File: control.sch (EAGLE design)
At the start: 103 parts, among them CN1 40PIN FPC, CN2 MINI B USB, CN3 0530471210, SW1 TACT, SW10 TACT, SW11 TACT, SW12 TACT, SW13 TACT, SW14 TACT, SW15 TACT, SW16 TACT, SW2 TACT, SW3 TACT, SW4 TACT, SW5 TACT, SW6 TACT, SW7 TACT, SW8 TACT, SW9 TACT, U1 STM32H743ZI, U2 AS4C8M16SA, U3 TPS61169DCKR, U4 USBLC6-2SC6, U5 FT230X, U6 DCDC 3V3

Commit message: Control nearly done
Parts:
- removed TP1, TP2: TEST_POINT_SQUARE, MISC:TEST_POINT_SQUARE
- added CN4: 2X10 HEADER, CONNECTORs:2X10_HEADER
- added R21: 10R, r_0603:ERJ3EKF10R0V
- CN3: value 0530471210 -> 2X10 HEADER; device CONNECTORs:PICOBLADE_12_TH_V -> CONNECTORs:2X10_HEADER
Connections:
- net JTAG_TRACECLK renamed N$5
- net JTAG_TRACED0 renamed N$6
- removed net 3V3D: CN3.3, CN3.4
- removed net DGND: CN3.10, CN3.11, CN3.12
- removed net DISP_!DE: CN1.34, U1.PF10
- removed net DISP_STBY: CN1.31
- removed net JTAG_TRACE: U1.PB3
- removed net N$101: U1.PB2
- removed net N$103: U1.PB4
- removed net N$111: U1.PB12
- removed net N$112: U1.PB13
- removed net N$120: U1.PC5
- removed net N$123: U1.PC8
- removed net N$128: U1.PC13
- removed net N$129: U1.PC14
- removed net N$130: U1.PC15
- removed net N$142: U1.PD11
- removed net N$143: U1.PD12
- removed net N$144: U1.PD13
- removed net N$169: U1.PF9
- removed net N$170: U1.PF8
- removed net N$171: U1.PF7
- removed net N$191: U1.PG3
- removed net N$192: U1.PG2
- removed net N$3: U1.PC4
- removed net N$47: C27.2, R3.1
- removed net N$49: C28.2, R4.1
- removed net N$5 (its old number): TP2.P$1, U6.VIN-
- removed net N$51: C29.2, R5.1
- removed net N$53: C30.2, R6.1
- removed net N$55: C31.2, R7.1
- removed net N$57: C32.2, R8.1
- removed net N$59: C33.2, R9.1
- removed net N$61: C34.2, R10.1
- removed net N$63: C35.2, R11.1
- removed net N$65: C36.2, R12.1
- removed net N$67: C37.2, R13.1
- removed net N$69: C38.2, R14.1
- removed net N$71: C39.2, R15.1
- removed net N$73: C40.2, R16.1
- removed net N$75: C41.2, R17.1
- removed net N$77: C42.2, R18.1
- new net BTN_0: C40.2, R16.1, U1.PC15
- new net BTN_1: C31.2, R7.1, U1.PD11
- new net BTN_2: C34.2, R10.1, R21.2, U1.PF9
- new net BTN_3: C37.2, R13.1, U1.PF7
- new net BTN_4: C30.2, R6.1, U1.PD12
- new net BTN_5: C33.2, R9.1, U1.PB12
- new net BTN_6: C36.2, R12.1, U1.PC4
- new net BTN_7: C29.2, R5.1, U1.PD13
- new net BTN_8: C32.2, R8.1, U1.PB13
- new net BTN_9: C35.2, R11.1, U1.PF8
- new net BTN_AMPS: C41.2, R17.1, U1.PC13
- new net BTN_CANCEL: C38.2, R14.1, U1.PC14
- new net BTN_DP: C39.2, R15.1, U1.PC5
- new net BTN_ON0FF: C27.2, R3.1, U1.PG3
- new net BTN_OUT_CONT: C28.2, R4.1, U1.PG2
- new net BTN_VOLTS: C42.2, R18.1, U1.PB2
- new net DISP_EN: CN1.31, U1.PC8
- new net JTAG_TDO: CN3.7, U1.PB3
- new net JTAG_TRST: CN3.2, U1.PB4
- new net PGND: CN4.10, CN4.11, CN4.12, CN4.9, U6.VIN-
- new net VIN: CN4.13, CN4.14, CN4.7, CN4.8, U6.VIN+
- net 3V3: now also CN3.1, CN4.19, CN4.2
- net ADC_!DRDY: now also CN4.5; no longer CN3.7
- net ADC_SPI_!CS: now also CN4.15; no longer CN3.8
- net ADC_SPI_MISO: now also CN4.4; no longer CN3.6
- net ADC_SPI_MOSI: now also CN4.3; no longer CN3.5
- net ADC_SPI_SCLK: now also CN4.6; no longer CN3.9
- net DAC_I2C_SCL: now also CN4.17; no longer CN3.1
- net DAC_I2C_SDA: now also CN4.18; no longer CN3.2
- net DISP_DE: now also CN1.34, U1.PF10; no longer U1.PF6
- net GND: now also CN3.11, CN3.12, CN3.13, CN3.14, CN3.15, CN3.16, CN3.17, CN3.18, CN3.19, CN3.6, CN4.1, CN4.16, CN4.20
- net JTAG_TCK: now also CN3.5
- net JTAG_TDI: now also CN3.3
- net JTAG_TMS: now also CN3.4
- net N$4: now also U1.PF6; no longer TP1.P$1, U6.VIN+
- net STM_BOOT0: now also R21.1
- net STM_NRST: now also CN3.8

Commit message: Checked against Cube
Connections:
- removed net N$104: U1.PB5
- removed net N$125: U1.PC10
- removed net N$126: U1.PC11
- removed net N$127: U1.PC12
- removed net N$133: U1.PD2
- removed net N$135: U1.PD4
- removed net N$136: U1.PD5
- removed net N$138: U1.PD7
- removed net N$161: U1.PE1
- removed net N$162: U1.PE0
- removed net N$180: U1.PG14
- removed net N$183: U1.PG11
- removed net N$4: U1.PF6
- removed net N$5: U1.PE2
- removed net N$6: U1.PE3
- removed net N$84: U1.PC1
- removed net N$95: U1.PA12
- net ADC_!DRDY: now also U1.PC1
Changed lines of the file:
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@@
-</segment>
-</net>
-<net name="N$95" class="0">
-<segment>
-<pinref part="U1" gate="G$1" pin="PA12"/>
-<wire x1="104.14" y1="226.06" x2="73.66" y2="226.06" width="0.1524" layer="91"/>
 </segment>
 </net>
@@
 </segment>
 </net>
-<net name="N$104" class="0">
-<segment>
-<pinref part="U1" gate="G$1" pin="PB5"/>
-<wire x1="104.14" y1="200.66" x2="73.66" y2="200.66" width="0.1524" layer="91"/>
-</segment>
-</net>
 <net name="DAC_I2C_SCL" class="0">
 <segment>
@@
 </segment>
 </net>
-<net name="N$125" class="0">
-<segment>
-<pinref part="U1" gate="G$1" pin="PC10"/>
-<wire x1="104.14" y1="144.78" x2="73.66" y2="144.78" width="0.1524" layer="91"/>
-</segment>
-</net>
-<net name="N$126" class="0">
-<segment>
-<pinref part="U1" gate="G$1" pin="PC11"/>
-<wire x1="104.14" y1="142.24" x2="73.66" y2="142.24" width="0.1524" layer="91"/>
-</segment>
-</net>
-<net name="N$127" class="0">
-<segment>
-<pinref part="U1" gate="G$1" pin="PC12"/>
-<wire x1="104.14" y1="139.7" x2="73.66" y2="139.7" width="0.1524" layer="91"/>
-</segment>
-</net>
 <net name="BTN_AMPS" class="0">
 <segment>
@@
 </segment>
 </net>
-<net name="N$133" class="0">
-<segment>
-<pinref part="U1" gate="G$1" pin="PD2"/>
-<wire x1="104.14" y1="121.92" x2="73.66" y2="121.92" width="0.1524" layer="91"/>
-</segment>
-</net>
-<net name="N$135" class="0">
-<segment>
-<pinref part="U1" gate="G$1" pin="PD4"/>
-<wire x1="104.14" y1="116.84" x2="73.66" y2="116.84" width="0.1524" layer="91"/>
-</segment>
-</net>
-<net name="N$136" class="0">
-<segment>
-<pinref part="U1" gate="G$1" pin="PD5"/>
-<wire x1="104.14" y1="114.3" x2="73.66" y2="114.3" width="0.1524" layer="91"/>
-</segment>
-</net>
-<net name="N$138" class="0">
-<segment>
-<pinref part="U1" gate="G$1" pin="PD7"/>
-<wire x1="104.14" y1="109.22" x2="73.66" y2="109.22" width="0.1524" layer="91"/>
-</segment>
-</net>
 <net name="SDRAM_D13" class="0">
 <segment>
@@
 </segment>
 </net>
-<net name="N$161" class="0">
-<segment>
-<pinref part="U1" gate="G$1" pin="PE1"/>
-<wire x1="144.78" y1="124.46" x2="175.26" y2="124.46" width="0.1524" layer="91"/>
-</segment>
-</net>
-<net name="N$162" class="0">
-<segment>
-<pinref part="U1" gate="G$1" pin="PE0"/>
-<wire x1="144.78" y1="127" x2="175.26" y2="127" width="0.1524" layer="91"/>
-</segment>
-</net>
 <net name="SDRAM_A9" class="0">
 <segment>
@@
 </segment>
 </net>
-<net name="N$180" class="0">
-<segment>
-<pinref part="U1" gate="G$1" pin="PG14"/>
-<wire x1="144.78" y1="177.8" x2="175.26" y2="177.8" width="0.1524" layer="91"/>
-</segment>
-</net>
-<net name="N$183" class="0">
-<segment>
-<pinref part="U1" gate="G$1" pin="PG11"/>
-<wire x1="144.78" y1="185.42" x2="175.26" y2="185.42" width="0.1524" layer="91"/>
-</segment>
-</net>
 <net name="ADC_SPI_!CS" class="0">
 <segment>
@@
 <wire x1="289.56" y1="177.8" x2="259.08" y2="177.8" width="0.1524" layer="91"/>
 <label x="261.62" y="177.8" size="1.778" layer="95"/>
-</segment>
-</net>
-<net name="N$84" class="0">
-<segment>
-<pinref part="U1" gate="G$1" pin="PC1"/>
-<wire x1="104.14" y1="167.64" x2="73.66" y2="167.64" width="0.1524" layer="91"/>
 </segment>
 </net>
@@
 <label x="205.74" y="431.8" size="1.778" layer="95"/>
 </segment>
+<segment>
+<pinref part="U1" gate="G$1" pin="PC1"/>
+<wire x1="104.14" y1="167.64" x2="73.66" y2="167.64" width="0.1524" layer="91"/>
+<label x="76.2" y="167.64" size="1.778" layer="95"/>
+</segment>
 </net>
 <net name="BTN_6" class="0">
@@
 </segment>
 </net>
-<net name="N$4" class="0">
-<segment>
-<pinref part="U1" gate="G$1" pin="PF6"/>
-<wire x1="144.78" y1="154.94" x2="175.26" y2="154.94" width="0.1524" layer="91"/>
-</segment>
-</net>
-<net name="N$5" class="0">
-<segment>
-<pinref part="U1" gate="G$1" pin="PE2"/>
-<wire x1="144.78" y1="121.92" x2="175.26" y2="121.92" width="0.1524" layer="91"/>
-</segment>
-</net>
-<net name="N$6" class="0">
-<segment>
-<pinref part="U1" gate="G$1" pin="PE3"/>
-<wire x1="144.78" y1="119.38" x2="175.26" y2="119.38" width="0.1524" layer="91"/>
-</segment>
-</net>

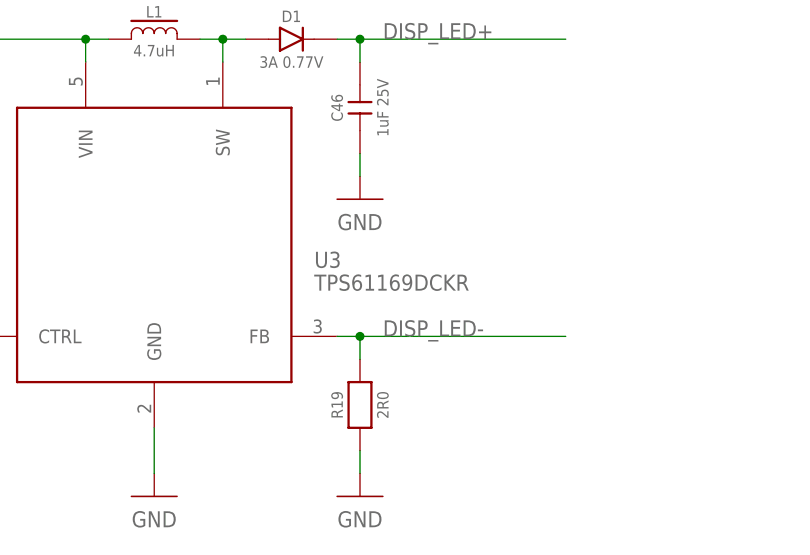
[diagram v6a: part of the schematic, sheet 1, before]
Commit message: Updated libs with digikey numbers
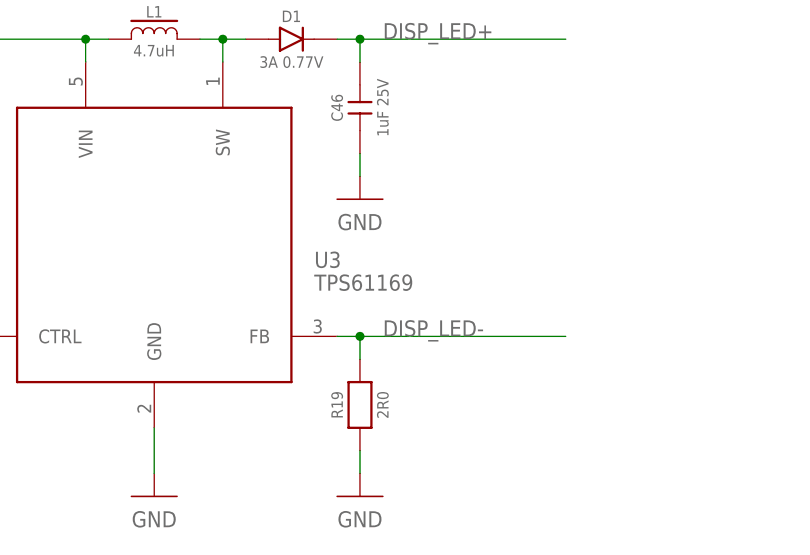
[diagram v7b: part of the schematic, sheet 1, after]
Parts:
- C45: device CAPACITORS:GRM188R60J475ME19D -> CAPACITORS:CL10B475KQ8NQNC
- U3: value TPS61169DCKR -> TPS61169
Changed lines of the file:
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@@
 <part name="GND49" library="NETS" deviceset="GND" device=""/>
 <part name="U$42" library="NETS" deviceset="3V3" device=""/>
-<part name="U3" library="ICs" deviceset="TPS61169" device="DCKR"/>
+<part name="U3" library="ICs" deviceset="TPS61169" device="DCKR" value="TPS61169"/>
 <part name="U6" library="ICs" deviceset="PDQE15-Q24-S3-D" device="" value="DCDC 3V3"/>
-<part name="C45" library="CAPACITORS" deviceset="GRM188R60J475ME19D" device="" value="4.7uF 6.3V"/>
+<part name="C45" library="CAPACITORS" deviceset="CL10B475KQ8NQNC" device="" value="4.7uF 6.3V"/>
 <part name="GND50" library="NETS" deviceset="GND" device=""/>
 <part name="GND51" library="NETS" deviceset="GND" device=""/>

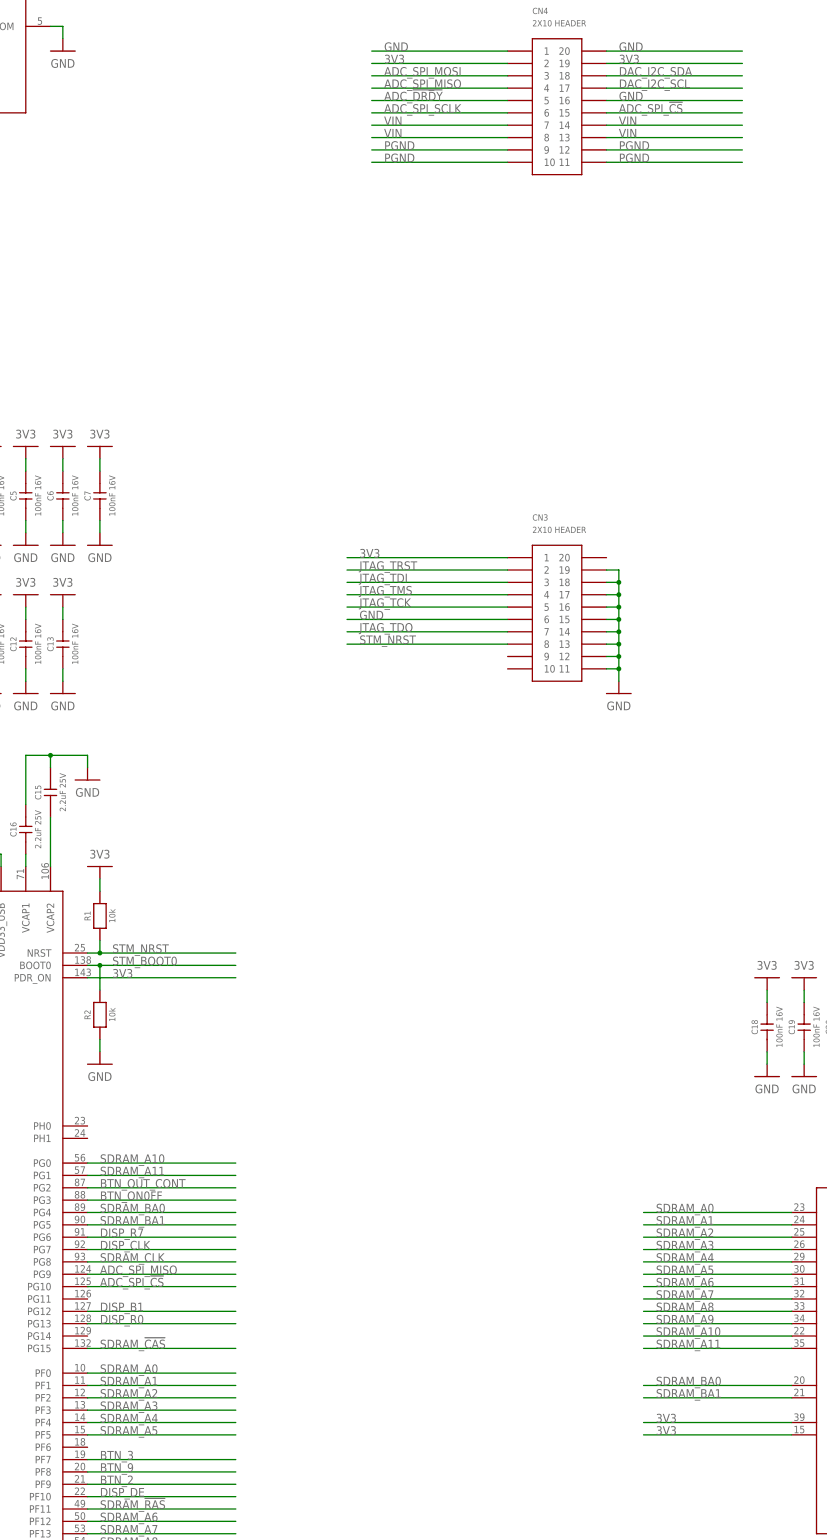
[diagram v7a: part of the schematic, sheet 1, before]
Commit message: Added control for the output relay
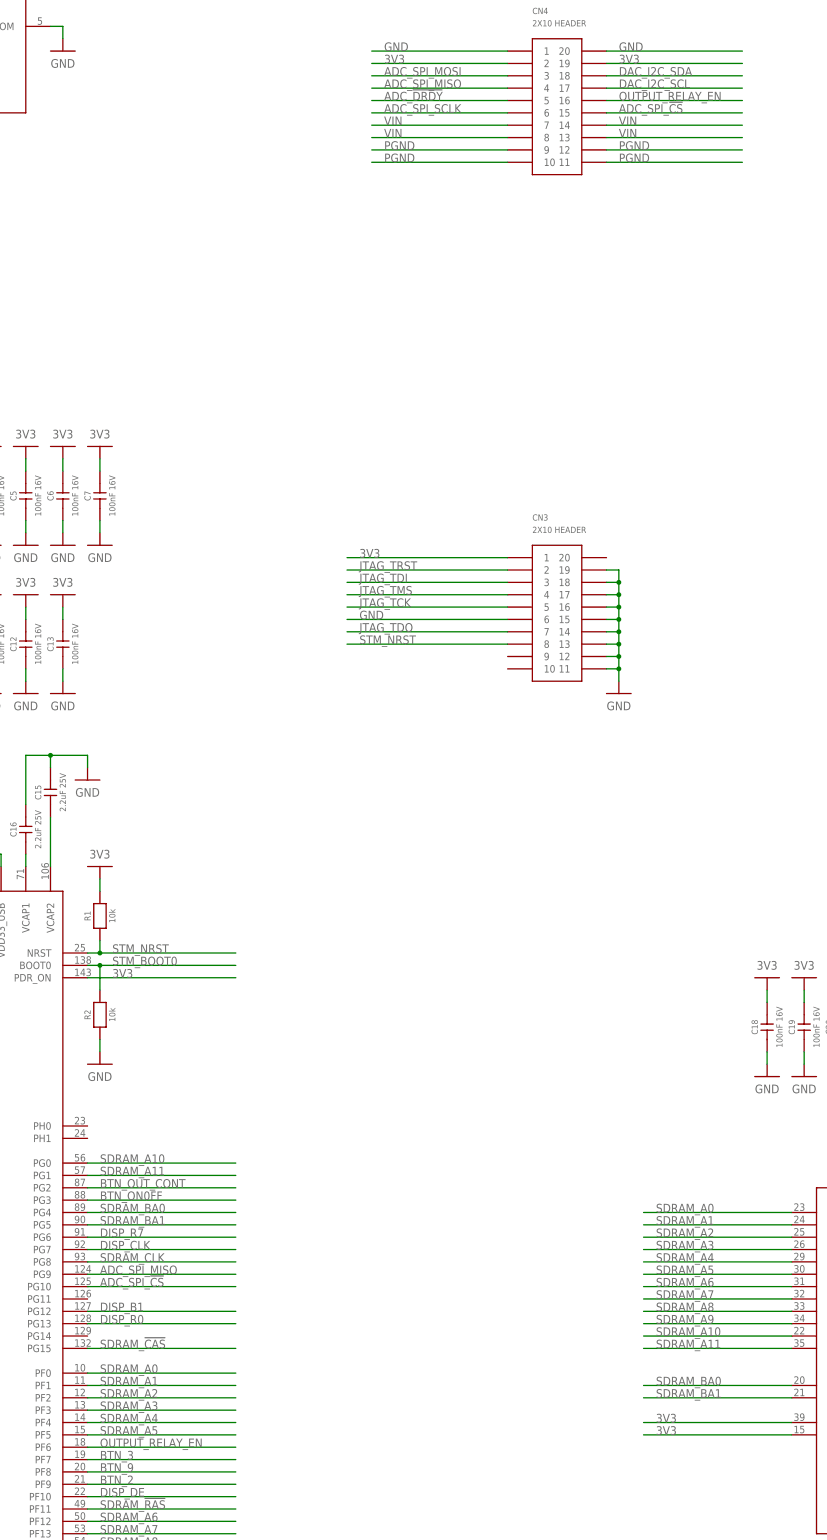
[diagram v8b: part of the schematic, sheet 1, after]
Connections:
- new net OUTPUT_RELAY_EN: CN4.16, U1.PF6
- net GND: no longer CN4.16
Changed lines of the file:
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@@
-</segment>
-<segment>
-<pinref part="CN4" gate="G$1" pin="16"/>
-<wire x1="251.46" y1="431.8" x2="279.4" y2="431.8" width="0.1524" layer="91"/>
-<label x="254" y="431.8" size="1.778" layer="95"/>
 </segment>
 <segment>
@@
 </segment>
 </net>
+<net name="OUTPUT_RELAY_EN" class="0">
+<segment>
+<pinref part="CN4" gate="G$1" pin="16"/>
+<wire x1="251.46" y1="431.8" x2="279.4" y2="431.8" width="0.1524" layer="91"/>
+<label x="254" y="431.8" size="1.778" layer="95"/>
+</segment>
+<segment>
+<pinref part="U1" gate="G$1" pin="PF6"/>
+<wire x1="144.78" y1="154.94" x2="175.26" y2="154.94" width="0.1524" layer="91"/>
+<label x="147.32" y="154.94" size="1.778" layer="95"/>
+</segment>
+</net>
